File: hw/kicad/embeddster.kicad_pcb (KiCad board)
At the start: 2 copper layers, 1 part, among them U1 ESP32-DEVKIT-V1

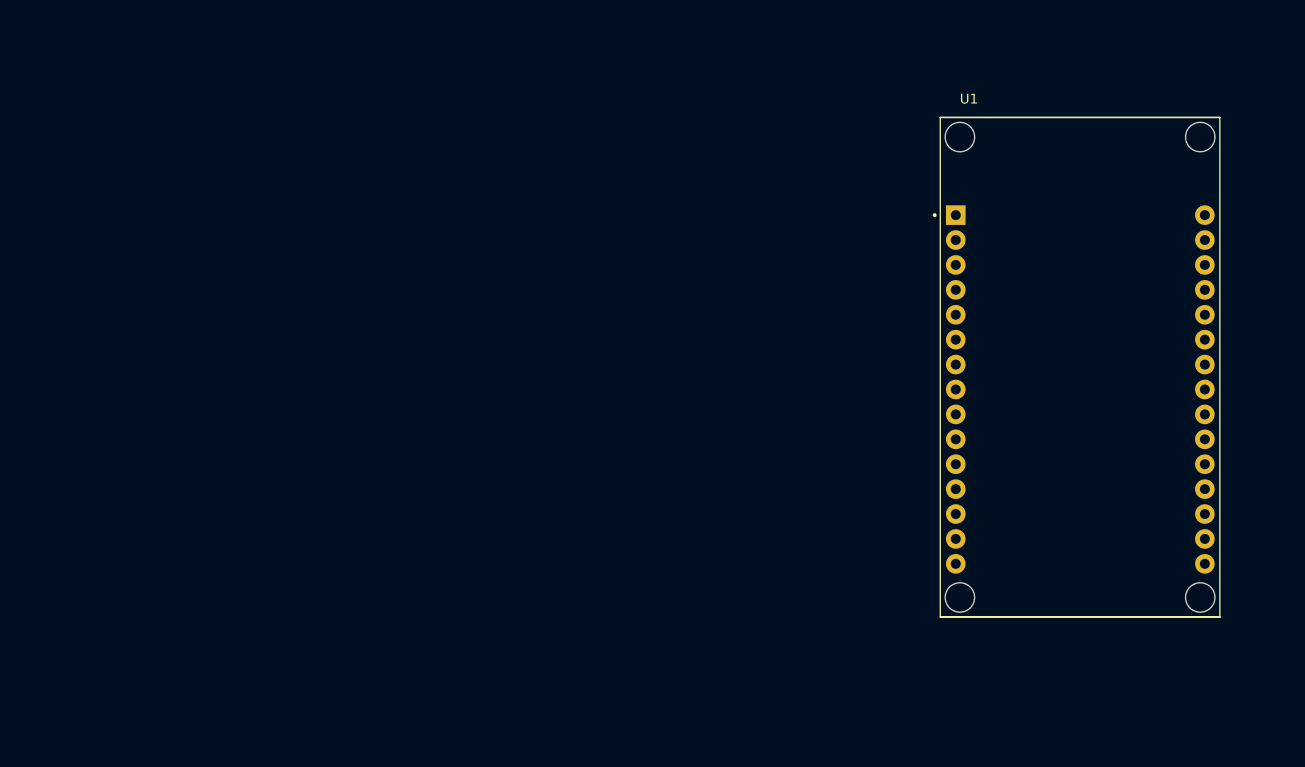
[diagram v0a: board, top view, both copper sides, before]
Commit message: Pcb v0 (#1)
* Add custom KiCad symbol&footproint for PLACA_CAN_V20190517

* Add 3D models for PLACA_CAN_V20190517 connector pins

* Remove mounting holes from ESP32 footprint

* sch supporting tp1 & tp2

* Remove unnecessary zone definitions from ESP32 DevKit V1 footprint

* Add 3D models for ESP32 DevKit V1 connector pins

* pcb ready for fab

* Add pin assignment header for MCP, encoder, and 74HC595 control, based on PCB

* Add 4th quantum standoff to PCB, ground plane adjustments

* Add a WS2812B cell

* Add active low definition for encoder switch

* Update README to remove TP3 reference and clarify hardware interface

* Fix routing, remove old pic

* re-fix routing
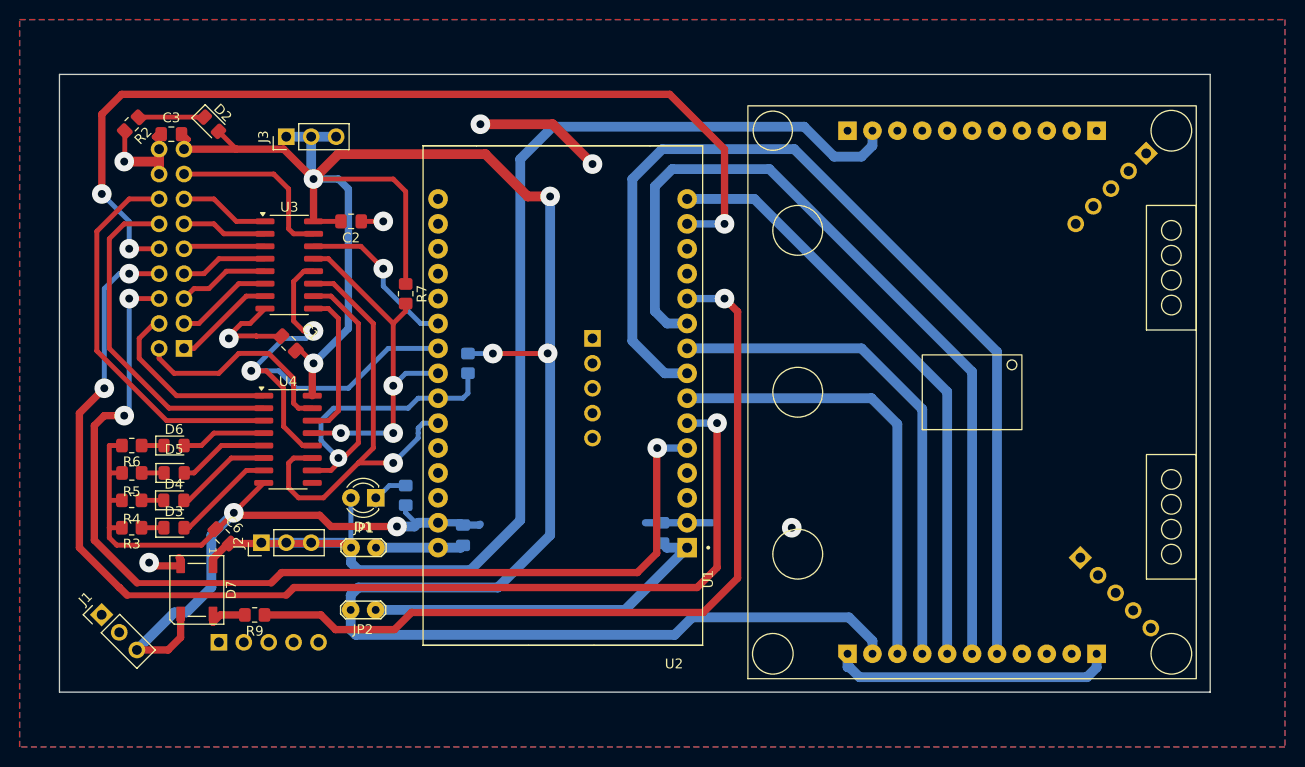
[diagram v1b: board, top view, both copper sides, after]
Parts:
- added C1: 100n, Capacitor_SMD:C_0805_2012Metric_Pad1.18x1.45mm_HandSolder, F.Cu at (108.7, 67.6)
- added C2: 100n, Capacitor_SMD:C_0805_2012Metric_Pad1.18x1.45mm_HandSolder, F.Cu at (115.1, 55.1)
- added C3: 100n, Capacitor_SMD:C_0805_2012Metric_Pad1.18x1.45mm_HandSolder, F.Cu at (96.8, 46.2)
- added C4: 100n, Capacitor_SMD:C_0805_2012Metric_Pad1.18x1.45mm_HandSolder, B.Cu at (126.5, 87.1)
- added C5: 100n, Capacitor_SMD:C_0805_2012Metric_Pad1.18x1.45mm_HandSolder, B.Cu at (146.8, 86.9)
- added C6: 100n, Capacitor_SMD:C_0805_2012Metric_Pad1.18x1.45mm_HandSolder, F.Cu at (102.0, 87.2)
- added D1: LED, LED_THT:LED_D3.0mm, F.Cu at (117.6, 83.3)
- added D2: LED, LED_SMD:LED_0805_2012Metric_Pad1.15x1.40mm_HandSolder, F.Cu at (100.8, 45.2)
- added D3: LED, LED_SMD:LED_0805_2012Metric_Pad1.15x1.40mm_HandSolder, F.Cu at (97.0, 86.4)
- added D4: LED, LED_SMD:LED_0805_2012Metric_Pad1.15x1.40mm_HandSolder, F.Cu at (97.0, 83.6)
- added D5: LED, LED_SMD:LED_0805_2012Metric_Pad1.15x1.40mm_HandSolder, F.Cu at (97.0, 80.8)
- added D6: LED, LED_SMD:LED_0805_2012Metric_Pad1.15x1.40mm_HandSolder, F.Cu at (97.0, 78.0)
- added D7: WS2812B, LED_SMD:LED_WS2812B_PLCC4_5.0x5.0mm_P3.2mm, F.Cu at (99.3, 92.7)
- added J1: Conn_01x03_Pin, Connector_PinHeader_2.54mm:PinHeader_1x03_P2.54mm_Vertical, F.Cu at (89.6, 95.2)
- added J2: Conn_01x03_Pin, Connector_PinHeader_2.54mm:PinHeader_1x03_P2.54mm_Vertical, F.Cu at (105.9, 87.9)
- added J3: Conn_01x03_Pin, Connector_PinHeader_2.54mm:PinHeader_1x03_P2.54mm_Vertical, F.Cu at (108.5, 46.5)
- added J4: TP1_CONN, Connector_PinSocket_2.54mm:PinSocket_2x09_P2.54mm_Vertical, B.Cu at (98.0, 68.1)
- added J5: Conn_01x05_Socket, Connector_PinSocket_2.54mm:PinSocket_1x05_P2.54mm_Vertical, B.Cu at (101.6, 98.0)
- added J6: Conn_01x05_Socket, Connector_PinSocket_2.54mm:PinSocket_1x05_P2.54mm_Vertical, B.Cu at (196.2, 48.2)
- added J7: Conn_01x05_Socket, Connector_PinSocket_2.54mm:PinSocket_1x05_P2.54mm_Vertical, B.Cu at (189.5, 89.4)
- added J8: Conn_01x05_Socket, Connector_PinSocket_2.54mm:PinSocket_1x05_P2.54mm_Vertical, B.Cu at (139.7, 67.1)
- added JP1: Jumper_2_Open, TestPoint:TestPoint_2Pads_Pitch2.54mm_Drill0.8mm, F.Cu at (115.1, 88.4)
- added JP2: Jumper_2_Open, TestPoint:TestPoint_2Pads_Pitch2.54mm_Drill0.8mm, F.Cu at (117.6, 94.7)
- added R1: 680, Resistor_SMD:R_0805_2012Metric_Pad1.20x1.40mm_HandSolder, B.Cu at (120.7, 83.1)
- added R2: 470, Resistor_SMD:R_0805_2012Metric_Pad1.20x1.40mm_HandSolder, F.Cu at (92.7, 45.2)
- added R3: 220, Resistor_SMD:R_0805_2012Metric_Pad1.20x1.40mm_HandSolder, F.Cu at (92.7, 86.4)
- added R4: 220, Resistor_SMD:R_0805_2012Metric_Pad1.20x1.40mm_HandSolder, F.Cu at (92.7, 83.6)
- added R5: 220, Resistor_SMD:R_0805_2012Metric_Pad1.20x1.40mm_HandSolder, F.Cu at (92.7, 80.8)
- added R6: 220, Resistor_SMD:R_0805_2012Metric_Pad1.20x1.40mm_HandSolder, F.Cu at (92.7, 78.0)
- added R7: 10k, Resistor_SMD:R_0805_2012Metric_Pad1.20x1.40mm_HandSolder, F.Cu at (120.7, 62.5)
- added R8: 10k, Resistor_SMD:R_0805_2012Metric_Pad1.20x1.40mm_HandSolder, B.Cu at (127.0, 69.6)
- added R9: 470, Resistor_SMD:R_0805_2012Metric_Pad1.20x1.40mm_HandSolder, F.Cu at (105.2, 95.2)
- added U1: PLACA_CAN_V20190517, PLACA_CAN_V20190517:PLACA_CAN_V20190517, F.Cu at (155.5, 101.8)
- added U3: 74HC595, Package_SO:SOIC-16_3.9x9.9mm_P1.27mm, F.Cu at (108.8, 59.6)
- added U4: 74HC595, Package_SO:SOIC-16_3.9x9.9mm_P1.27mm, F.Cu at (108.6, 77.3)
- moved U2 52.9 mm to (136.7, 72.9), turned to 180 degrees
- renumbered U1 to U2
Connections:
- net Net-(U1-GND-Pad2) renamed GND
- U2 pad 1: unconnected-(U1-3V3-Pad1) -> Net-(JP2-A)
- U2 pad 10: unconnected-(U1-D19-Pad10) -> /CAN_MISO
- U2 pad 11: unconnected-(U1-D21-Pad11) -> /NPXL
- U2 pad 14: unconnected-(U1-D22-Pad14) -> /TP1_RSWITCH
- U2 pad 15: unconnected-(U1-D23-Pad15) -> /CAN_MOSI
- U2 pad 21: unconnected-(U1-D32-Pad21) -> /595_SI
- U2 pad 22: unconnected-(U1-D33-Pad22) -> /595_LATCH_CLK
- U2 pad 23: unconnected-(U1-D25-Pad23) -> /595_nOE
- U2 pad 24: unconnected-(U1-D26-Pad24) -> /595_nRST
- U2 pad 25: unconnected-(U1-D27-Pad25) -> /595_SHIFT_CLK
- U2 pad 30: unconnected-(U1-VIN-Pad30) -> Net-(JP1-B)
- U2 pad 5: unconnected-(U1-D4-Pad5) -> /TP1_RCHA
- U2 pad 6: unconnected-(U1-RX2-Pad6) -> /TP1_RCHB
- U2 pad 7: unconnected-(U1-TX2-Pad7) -> /CAN_nINT
- U2 pad 8: unconnected-(U1-D5-Pad8) -> /CAN_nCS
- U2 pad 9: unconnected-(U1-D18-Pad9) -> /CAN_SCK
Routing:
- net +3V3: track 0.00 -> 236.0 mm, vias 0 -> 5
- net GND: track 0.00 -> 160.5 mm, vias 0 -> 8
- net +5V: track 0.00 -> 128.6 mm
- net /TP1_RCHB: track 0.00 -> 119.7 mm, vias 0 -> 3
- net /TP1_RCHA: track 0.00 -> 104.6 mm, vias 0 -> 3
- net /CAN_nCS: track 0.00 -> 101.3 mm
- net /TP1_RSWITCH: track 0.00 -> 96.0 mm, vias 0 -> 3
- net /CAN_MISO: track 0.00 -> 86.9 mm
- net /NPXL: track 0.00 -> 83.9 mm, vias 0 -> 1
- net /CAN_MOSI: track 0.00 -> 61.4 mm
- net /CAN_SCK: track 0.00 -> 51.5 mm
- net /595_LATCH_CLK: track 0.00 -> 50.1 mm, vias 0 -> 2
- net /595_SHIFT_CLK: track 0.00 -> 47.2 mm, vias 0 -> 1
- net /595_nRST: track 0.00 -> 46.5 mm, vias 0 -> 1
- net /CAN_nINT: track 0.00 -> 46.0 mm
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- added copper zone on B.Cu, net GND
- added copper zone on F.Cu, net GND
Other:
- board outline added: 117.3 x 63 mm
